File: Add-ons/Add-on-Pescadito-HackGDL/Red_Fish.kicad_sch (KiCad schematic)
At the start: 16 parts, among them J1 Conn_02x03_Odd_Even, SW1 SW_RST, SW2 On, U1 PY32F002AA15M6TU

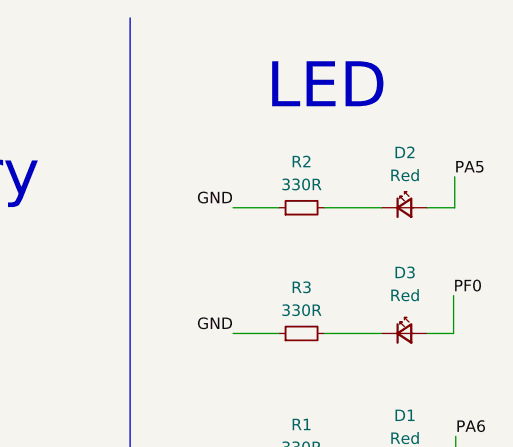
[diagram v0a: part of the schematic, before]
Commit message: feat(Hw):Update_Labels
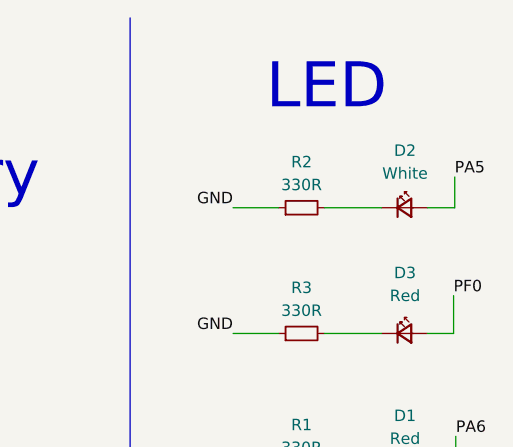
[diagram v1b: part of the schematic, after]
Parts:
- D2: value Red -> White; LCSC# C965812 -> C84258
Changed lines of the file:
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@@
 		(fields_autoplaced yes)
 		(property "Reference" "D2"
-			(at 184.2135 26.924 0)
+			(at 184.2135 26.67 0)
 			(effects
 				(font
@@
 			)
 		)
-		(property "Value" "Red"
-			(at 184.2135 29.464 0)
+		(property "Value" "White"
+			(at 184.2135 29.21 0)
 			(effects
 				(font
@@
 			)
 		)
-		(property "LCSC#" "C965812"
+		(property "LCSC#" "C84258"
 			(at 184.15 33.02 0)
 			(effects
